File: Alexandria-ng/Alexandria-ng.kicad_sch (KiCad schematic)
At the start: 28 parts, among them SW1 SW_Push_Dual, U1 RTL8367S-CG, Y1 25M

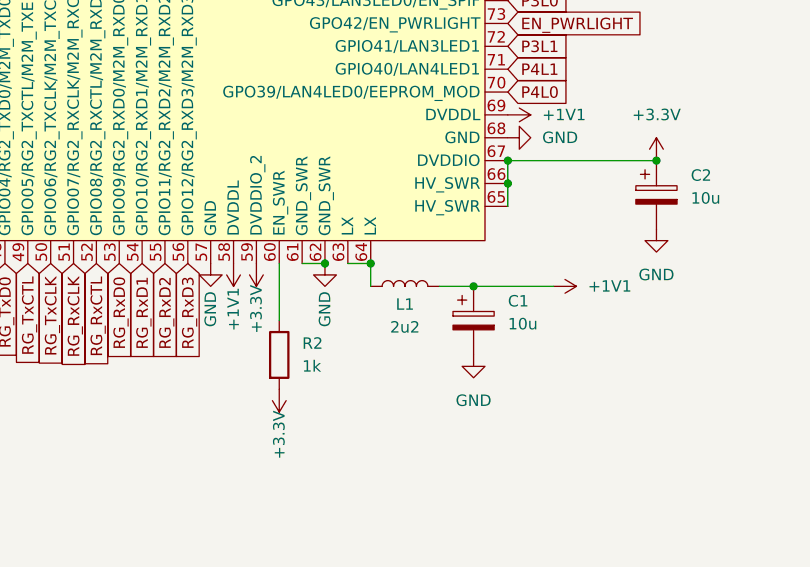
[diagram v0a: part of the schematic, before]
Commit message: Update to KiCad 7.0, add footprint to RJ45 jacks
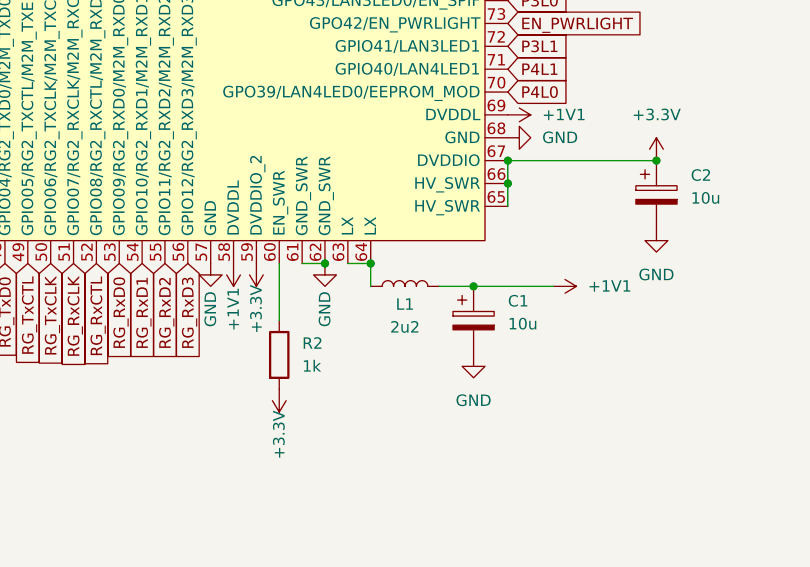
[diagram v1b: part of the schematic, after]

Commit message: Annotate & assign footprints
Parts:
- D2: footprint (none) -> Diode_SMD:D_MiniMELF_Handsoldering
- F1: footprint (none) -> Fuse:Fuse_0603_1608Metric_Pad1.05x0.95mm_HandSolder
- L1: footprint (none) -> Inductor_SMD:L_Ferrocore_DLG-0504
- SW1: footprint (none) -> Button_Switch_SMD:SW_Push_1P1T_NO_6x6mm_H9.5mm
- gave numbers to parts that had none: 1
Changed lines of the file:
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@@
   (symbol (lib_id "Device:R") (at 215.9 109.22 90) (unit 1)
     (in_bom yes) (on_board yes) (dnp no) (fields_autoplaced)
-    (property "Reference" "R?" (at 215.9 102.87 90)
+    (property "Reference" "R53" (at 215.9 102.87 90)
       (effects (font (size 1.27 1.27)))
     )
@@
       (project "Alexandria-ng"
         (path "/d75cf6f5-5ddc-4328-8d5c-12d6ef92ffe7"
-          (reference "R?") (unit 1)
+          (reference "R53") (unit 1)
         )
       )
@@
       (effects (font (size 1.27 1.27)) (justify left))
     )
-    (property "Footprint" "" (at 238.76 113.03 0)
+    (property "Footprint" "Diode_SMD:D_MiniMELF_Handsoldering" (at 238.76 113.03 0)
       (effects (font (size 1.27 1.27)) hide)
     )
@@
   (symbol (lib_id "power:+2V8") (at 208.28 109.22 0) (unit 1)
     (in_bom yes) (on_board yes) (dnp no) (fields_autoplaced)
-    (property "Reference" "#PWR?" (at 208.28 113.03 0)
+    (property "Reference" "#PWR0101" (at 208.28 113.03 0)
       (effects (font (size 1.27 1.27)) hide)
     )
@@
       (project "Alexandria-ng"
         (path "/d75cf6f5-5ddc-4328-8d5c-12d6ef92ffe7"
-          (reference "#PWR?") (unit 1)
+          (reference "#PWR0101") (unit 1)
         )
       )
@@
       (effects (font (size 1.27 1.27)))
     )
-    (property "Footprint" "" (at 220.98 97.79 0)
+    (property "Footprint" "Fuse:Fuse_0603_1608Metric_Pad1.05x0.95mm_HandSolder" (at 220.98 97.79 0)
       (effects (font (size 1.27 1.27)) (justify left) hide)
     )
@@
       (effects (font (size 1.27 1.27)) (justify bottom))
     )
-    (property "Footprint" "" (at 137.16 142.24 0)
+    (property "Footprint" "Inductor_SMD:L_Ferrocore_DLG-0504" (at 137.16 142.24 0)
       (effects (font (size 1.27 1.27)) hide)
     )
@@
       (effects (font (size 1.27 1.27)) (justify right))
     )
-    (property "Footprint" "" (at 212.09 151.13 0)
-      (effects (font (size 1.27 1.27)) hide)
-    )
+    (property "Footprint" "Button_Switch_SMD:SW_Push_1P1T_NO_6x6mm_H9.5mm" (at 212.09 151.13 0)
+      (effects (font (size 1.27 1.27)) hide)
+    )

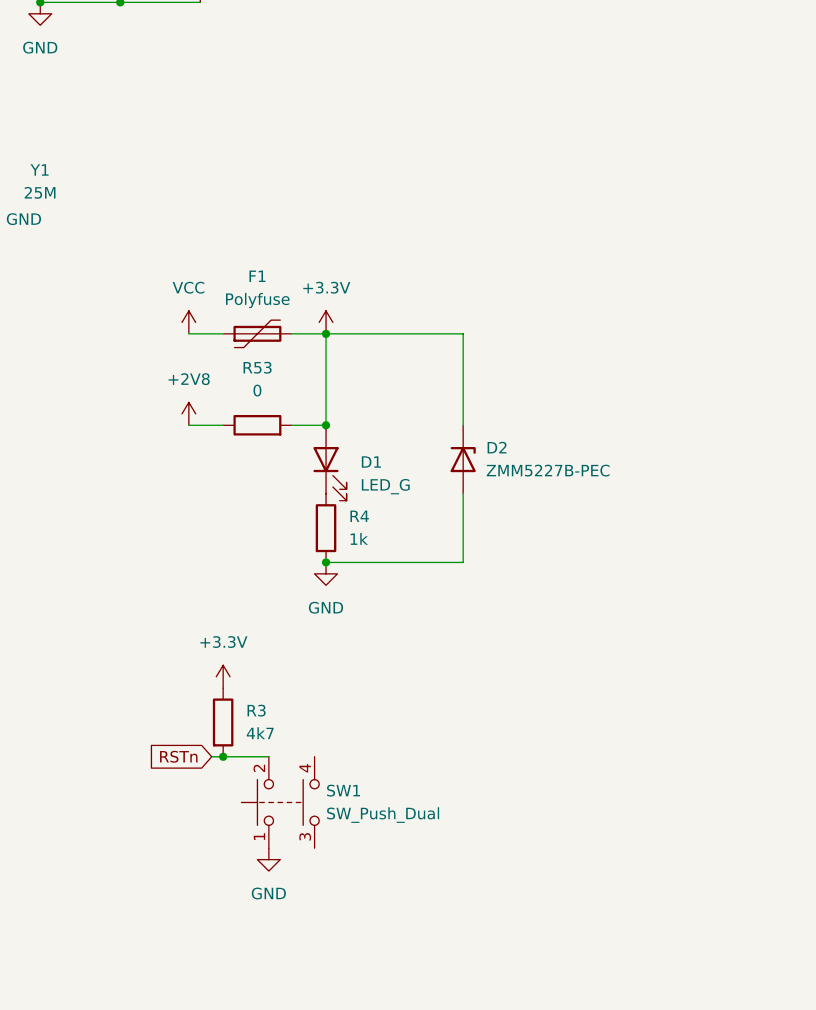
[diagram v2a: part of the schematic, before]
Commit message: Re-do VCC and RST, add VCC connector
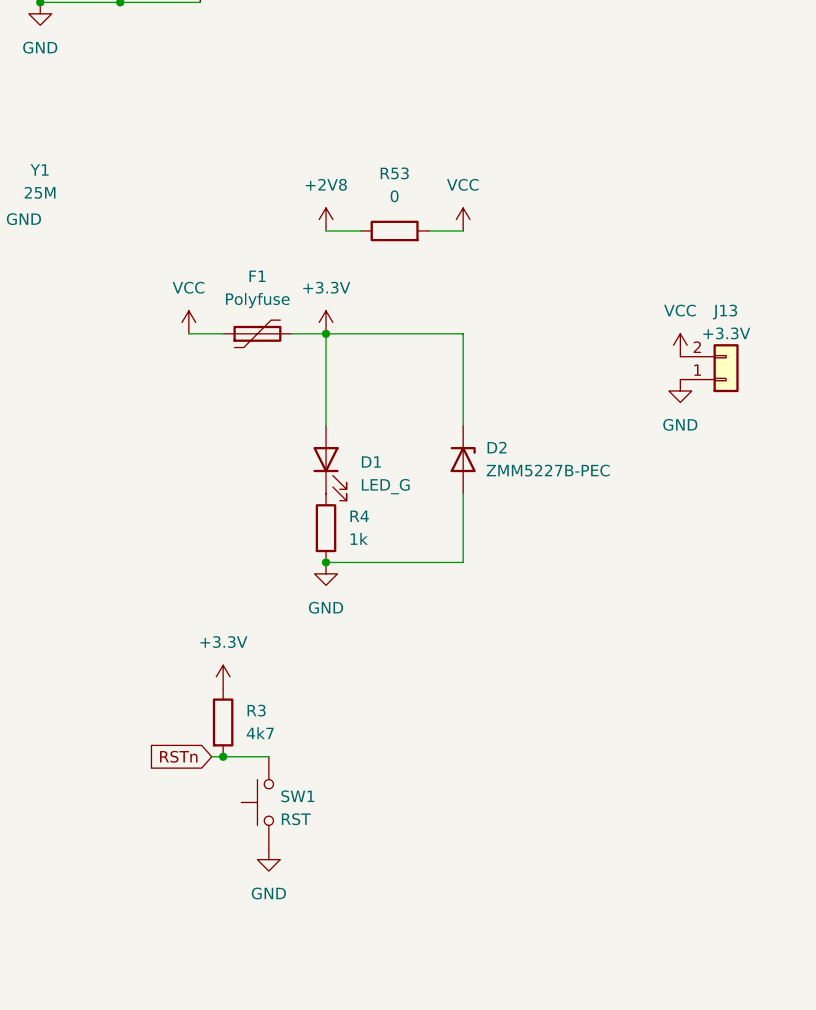
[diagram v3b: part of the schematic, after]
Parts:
- removed SW1: SW_Push_Dual, Button_Switch_SMD:SW_Push_1P1T_NO_6x6mm_H9.5mm, symbol Switch:SW_Push_Dual
- added J13: +3.3V, Connector_PinHeader_2.54mm:PinHeader_1x02_P2.54mm_Vertical, symbol Connector_Generic:Conn_01x02
- added SW1: RST, Button_Switch_SMD:SW_Push_1P1T_NO_6x6mm_H9.5mm, symbol Switch:SW_Push
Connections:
- net +3.3V: no longer R53.2
- net GND: now also J13.1 (Pin_1), SW1.1
- net RSTn: now also SW1.2
- net VCC: now also R53.2, J13.2 (Pin_2)
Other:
- moved on the sheet: R53
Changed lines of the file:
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@@
   (junction (at 165.1 128.27) (diameter 0) (color 0 0 0 0)
   )
-  (junction (at 223.52 109.22) (diameter 0) (color 0 0 0 0)
-  )
   (junction (at 236.22 21.59) (diameter 0) (color 0 0 0 0)
   )
@@
     (stroke (width 0) (type default))
   )
-  (wire (pts (xy 219.71 109.22) (xy 223.52 109.22))
+  (wire (pts (xy 234.95 87.63) (xy 238.76 87.63))
     (stroke (width 0) (type default))
   )
@@
     (stroke (width 0) (type default))
   )
-  (wire (pts (xy 212.09 109.22) (xy 208.28 109.22))
+  (wire (pts (xy 227.33 87.63) (xy 223.52 87.63))
     (stroke (width 0) (type default))
   )
@@
     )
   )
-  (symbol (lib_id "Device:R") (at 215.9 109.22 90) (unit 1)
-    (in_bom yes) (on_board yes) (dnp no) (fields_autoplaced)
-    (property "Reference" "R53" (at 215.9 102.87 90)
-      (effects (font (size 1.27 1.27)))
-    )
-    (property "Value" "0" (at 215.9 105.41 90)
-      (effects (font (size 1.27 1.27)))
-    )
-    (property "Footprint" "Resistor_SMD:R_0603_1608Metric_Pad0.98x0.95mm_HandSolder" (at 215.9 110.998 90)
-      (effects (font (size 1.27 1.27)) hide)
-    )
-    (property "Datasheet" "~" (at 215.9 109.22 0)
+  (symbol (lib_id "Device:R") (at 231.14 87.63 90) (unit 1)
+    (in_bom yes) (on_board yes) (dnp no) (fields_autoplaced)
+    (property "Reference" "R53" (at 231.14 81.28 90)
+      (effects (font (size 1.27 1.27)))
+    )
+    (property "Value" "0" (at 231.14 83.82 90)
+      (effects (font (size 1.27 1.27)))
+    )
+    (property "Footprint" "Resistor_SMD:R_0603_1608Metric_Pad0.98x0.95mm_HandSolder" (at 231.14 89.408 90)
+      (effects (font (size 1.27 1.27)) hide)
+    )
+    (property "Datasheet" "~" (at 231.14 87.63 0)
       (effects (font (size 1.27 1.27)) hide)
     )
@@
     )
   )
-  (symbol (lib_id "power:+2V8") (at 208.28 109.22 0) (unit 1)
-    (in_bom yes) (on_board yes) (dnp no) (fields_autoplaced)
-    (property "Reference" "#PWR0101" (at 208.28 113.03 0)
-      (effects (font (size 1.27 1.27)) hide)
-    )
-    (property "Value" "+2V8" (at 208.28 104.14 0)
-      (effects (font (size 1.27 1.27)))
-    )
-    (property "Footprint" "" (at 208.28 109.22 0)
-      (effects (font (size 1.27 1.27)) hide)
-    )
-    (property "Datasheet" "" (at 208.28 109.22 0)
+  (symbol (lib_id "power:+2V8") (at 223.52 87.63 0) (unit 1)
+    (in_bom yes) (on_board yes) (dnp no) (fields_autoplaced)
+    (property "Reference" "#PWR0101" (at 223.52 91.44 0)
+      (effects (font (size 1.27 1.27)) hide)
+    )
+    (property "Value" "+2V8" (at 223.52 82.55 0)
+      (effects (font (size 1.27 1.27)))
+    )
+    (property "Footprint" "" (at 223.52 87.63 0)
+      (effects (font (size 1.27 1.27)) hide)
+    )
+    (property "Datasheet" "" (at 223.52 87.63 0)
       (effects (font (size 1.27 1.27)) hide)
     )
@@
     )
   )
+  (symbol (lib_id "power:VCC") (at 238.76 87.63 0) (unit 1)
+    (in_bom yes) (on_board yes) (dnp no) (fields_autoplaced)
+    (property "Reference" "#PWR0102" (at 238.76 91.44 0)
+      (effects (font (size 1.27 1.27)) hide)
+    )
+    (property "Value" "VCC" (at 238.76 82.55 0)
+      (effects (font (size 1.27 1.27)))
+    )
+    (property "Footprint" "" (at 238.76 87.63 0)
+      (effects (font (size 1.27 1.27)) hide)
+    )
+    (property "Datasheet" "" (at 238.76 87.63 0)
+      (effects (font (size 1.27 1.27)) hide)
+    )
+    (pin "1")
+    (instances
+      (project "Alexandria-ng"
+        (path "/d75cf6f5-5ddc-4328-8d5c-12d6ef92ffe7"
+          (reference "#PWR0102") (unit 1)
+        )
+      )
+    )
+  )
   (symbol (lib_id "Device:R") (at 24.13 85.09 90) (unit 1)
     (in_bom yes) (on_board yes) (dnp no) (fields_autoplaced)
@@
         (path "/d75cf6f5-5ddc-4328-8d5c-12d6ef92ffe7"
           (reference "R1") (unit 1)
+        )
+      )
+    )
+  )
+  (symbol (lib_id "Switch:SW_Push") (at 217.17 151.13 90) (unit 1)
+    (in_bom yes) (on_board yes) (dnp no) (fields_autoplaced)
+    (property "Reference" "SW1" (at 218.44 150.495 90)
+      (effects (font (size 1.27 1.27)) (justify right))
+    )
+    (property "Value" "RST" (at 218.44 153.035 90)
+      (effects (font (size 1.27 1.27)) (justify right))
+    )
+    (property "Footprint" "Button_Switch_SMD:SW_Push_1P1T_NO_6x6mm_H9.5mm" (at 212.09 151.13 0)
+      (effects (font (size 1.27 1.27)) hide)
+    )
+    (property "Datasheet" "~" (at 212.09 151.13 0)
+      (effects (font (size 1.27 1.27)) hide)
+    )
+    (pin "1")
+    (pin "2")
+    (instances
+      (project "Alexandria-ng"
+        (path "/d75cf6f5-5ddc-4328-8d5c-12d6ef92ffe7"
+          (reference "SW1") (unit 1)
         )
       )
@@
     )
   )
+  (symbol (lib_id "power:VCC") (at 262.89 101.6 0) (unit 1)
+    (in_bom yes) (on_board yes) (dnp no) (fields_autoplaced)
+    (property "Reference" "#PWR0100" (at 262.89 105.41 0)
+      (effects (font (size 1.27 1.27)) hide)
+    )
+    (property "Value" "VCC" (at 262.89 96.52 0)
+      (effects (font (size 1.27 1.27)))
+    )
+    (property "Footprint" "" (at 262.89 101.6 0)
+      (effects (font (size 1.27 1.27)) hide)
+    )
+    (property "Datasheet" "" (at 262.89 101.6 0)
+      (effects (font (size 1.27 1.27)) hide)
+    )
+    (pin "1")
+    (instances
+      (project "Alexandria-ng"
+        (path "/d75cf6f5-5ddc-4328-8d5c-12d6ef92ffe7"
+          (reference "#PWR0100") (unit 1)
+        )
+      )
+    )
+  )
   (symbol (lib_id "power:GND") (at 184.15 86.36 90) (unit 1)
     (in_bom yes) (on_board yes) (dnp no) (fields_autoplaced)
@@
     )
   )
+  (symbol (lib_id "power:GND") (at 262.89 104.14 0) (unit 1)
+    (in_bom yes) (on_board yes) (dnp no) (fields_autoplaced)
+    (property "Reference" "#PWR099" (at 262.89 110.49 0)
+      (effects (font (size 1.27 1.27)) hide)
+    )
+    (property "Value" "GND" (at 262.89 109.22 0)
+      (effects (font (size 1.27 1.27)))
+    )
+    (property "Footprint" "" (at 262.89 104.14 0)
+      (effects (font (size 1.27 1.27)) hide)
+    )
+    (property "Datasheet" "" (at 262.89 104.14 0)
+      (effects (font (size 1.27 1.27)) hide)
+    )
+    (pin "1")
+    (instances
+      (project "Alexandria-ng"
+        (path "/d75cf6f5-5ddc-4328-8d5c-12d6ef92ffe7"
+          (reference "#PWR099") (unit 1)
+        )
+      )
+    )
+  )
   (symbol (lib_id "power:+3.3V") (at 191.77 21.59 0) (unit 1)
     (in_bom yes) (on_board yes) (dnp no) (fields_autoplaced)
@@
     )
   )
-  (symbol (lib_id "Switch:SW_Push_Dual") (at 217.17 151.13 90) (unit 1)
-    (in_bom yes) (on_board yes) (dnp no) (fields_autoplaced)
-    (property "Reference" "SW1" (at 223.52 149.8599 90)
-      (effects (font (size 1.27 1.27)) (justify right))
-    )
-    (property "Value" "SW_Push_Dual" (at 223.52 152.3999 90)
-      (effects (font (size 1.27 1.27)) (justify right))
-    )
-    (property "Footprint" "Button_Switch_SMD:SW_Push_1P1T_NO_6x6mm_H9.5mm" (at 212.09 151.13 0)
-      (effects (font (size 1.27 1.27)) hide)
-    )
-    (property "Datasheet" "~" (at 212.09 151.13 0)
-      (effects (font (size 1.27 1.27)) hide)
-    )
-    (pin "1")
-    (pin "2")
-    (pin "3")
-    (pin "4")
-    (instances
-      (project "Alexandria-ng"
-        (path "/d75cf6f5-5ddc-4328-8d5c-12d6ef92ffe7"
-          (reference "SW1") (unit 1)
-        )
-      )
-    )
-  )
   (symbol (lib_id "power:+1V1") (at 90.17 48.26 0) (unit 1)
     (in_bom yes) (on_board yes) (dnp no)
@@
         )
       )
+    )
+  )
+  (symbol (lib_id "Connector_Generic:Conn_01x02") (at 267.97 104.14 0) (mirror x) (unit 1)
+    (in_bom yes) (on_board yes) (dnp no)
+    (property "Reference" "J13" (at 267.97 96.52 0)
+      (effects (font (size 1.27 1.27)))
+    )
+    (property "Value" "+3.3V" (at 267.97 99.06 0)
+      (effects (font (size 1.27 1.27)))
+    )
+    (property "Footprint" "Connector_PinHeader_2.54mm:PinHeader_1x02_P2.54mm_Vertical" (at 267.97 104.14 0)
+      (effects (font (size 1.27 1.27)) hide)
+    )
+    (property "Datasheet" "~" (at 267.97 104.14 0)
+      (effects (font (size 1.27 1.27)) hide)
+    )
+    (pin "1")
+    (pin "2")
+    (instances
+      (project "Alexandria-ng"
+        (path "/d75cf6f5-5ddc-4328-8d5c-12d6ef92ffe7"
+          (reference "J13") (unit 1)
+        )
+      )

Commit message: Switch DVDDIO pins to +2.8V
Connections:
- net +2V8: now also R11.1, R12.1, R13.1, R14.1, R15.1, R16.1, R3.1, R5.1, R7.1, R9.1, U1.42 (DVDDIO_2), U1.59 (DVDDIO_2), U1.67 (DVDDIO)
- net +3.3V: no longer R11.1, R12.1, R13.1, R14.1, R15.1, R16.1, R3.1, R5.1, R7.1, R9.1, U1.42 (DVDDIO_2), U1.59 (DVDDIO_2), U1.67 (DVDDIO)
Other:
- moved on the sheet: C2
